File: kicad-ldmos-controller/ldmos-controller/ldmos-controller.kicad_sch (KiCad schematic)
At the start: 101 parts, among them J1 SWR1, J10 BCD Input, J11 LPF, J12 Digi In/Out, J13 12v/5v Outputs, J14 TX2/RX2, J15 TX0/RX0, J16 50v In., J17 PWM Out, J18 PTT IN, J19 DISPLAY POWER, J2 SWR2, J20 5V Output, J22 UDPI, J23 12v Output, J24 12v Output, J25 Temp 2, J3 I detect, J4 RF In Level, J5 50v In., J6 Temp, J7 Conn_01x03_Pin, J8 12v Input, J9 I2c Output, Q1 2n2222, U1 LTV-847, U2 MCP23017_SP, U3 LTV-847, U4 MIC2981/82YN, U5 MIC2981/82YN, U6 R-78E5.0-1.0

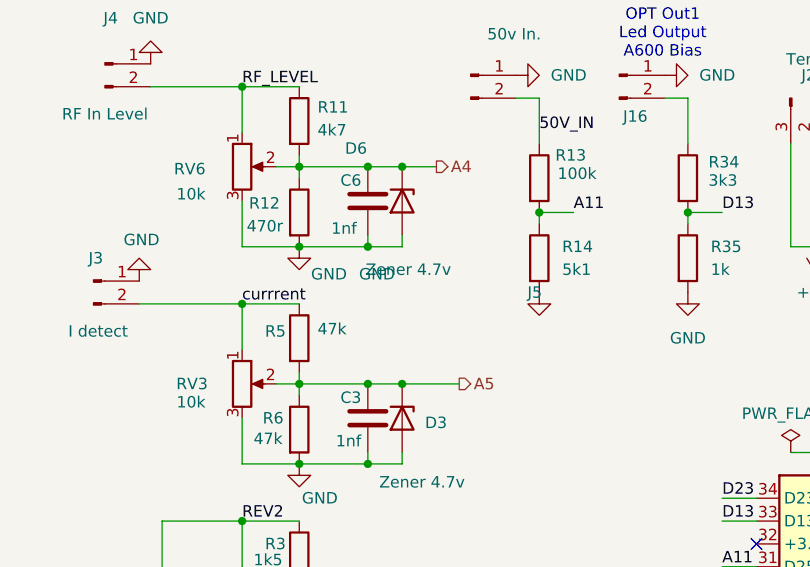
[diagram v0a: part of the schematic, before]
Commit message: update icons change 1 kicad component
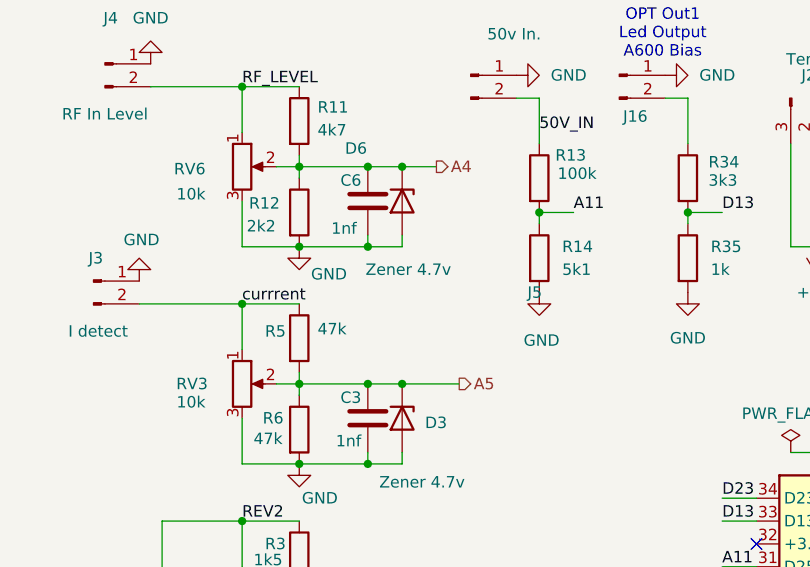
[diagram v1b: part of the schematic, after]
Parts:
- R12: value 470r -> 2k2
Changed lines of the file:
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@@
 		)
 		(property "Value" "GND"
-			(at 56.896 44.958 0)
+			(at 75.184 52.324 0)
 			(effects
 				(font
@@
 			)
 		)
-		(property "Value" "470r"
+		(property "Value" "2k2"
 			(at 42.418 39.624 0)
 			(effects
